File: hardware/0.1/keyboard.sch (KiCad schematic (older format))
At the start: 329 parts, among them J1 USB_C_Receptacle_USB2.0, J2 SWD, Q1 BSS138, Q3 DTC123J, SW1 SW_Push, U1 USBLC6-2SC6, U2 AP2112K-3.3, U3 STM32F303RCTx, Y1 8MHz

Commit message: add encoder top right
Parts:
- removed K_19: KEYSW, josh-keyboard:MXOnly-1U-NoLED, symbol josh-keyboard:MX-NoLED
- removed R7: 1K5, Resistor_SMD:R_0603_1608Metric, symbol Device:R
- added C31, C41: 100n, Capacitor_SMD:C_0603_1608Metric, symbol Device:C
- added K_19: Encoder_MX, josh-keyboard:MX_KEYSWITCH_ENCODER, symbol Device:Rotary_Encoder_Switch
- added RN5: 10K, Resistor_SMD:R_Array_Convex_4x0603, symbol josh-passive:RN
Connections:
- net +3V3: now also RN5.2, RN5.3
- net GND: now also C31.2, C41.2, K_19.C
- net col13: now also U3.17 (PA3); no longer U3.21 (PA5)
- net col19: now also K_19.S1
- net at D_19.2 (A): now also K_19.S2
- net ENC4_A_DB: now reaches U3.58 (PB6)
- net ENC4_A_DB: now also C31.1, RN5.4
- net ENC4_B_DB: now reaches U3.59 (PB7)
- net ENC4_B_DB: now also C41.1, RN5.1
- net MCU_RST: no longer names the net of U3.50 (PA15)
- new net ENC4_A: K_19.A, RN5.5, RN5.6
- new net ENC4_B: K_19.B, RN5.7, RN5.8
- no-connect marks 12 -> 11
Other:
- moved on the sheet: C10, C11, C12, C13, C6, C7, C8, C9, D_107, D_19, D_38, D_58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

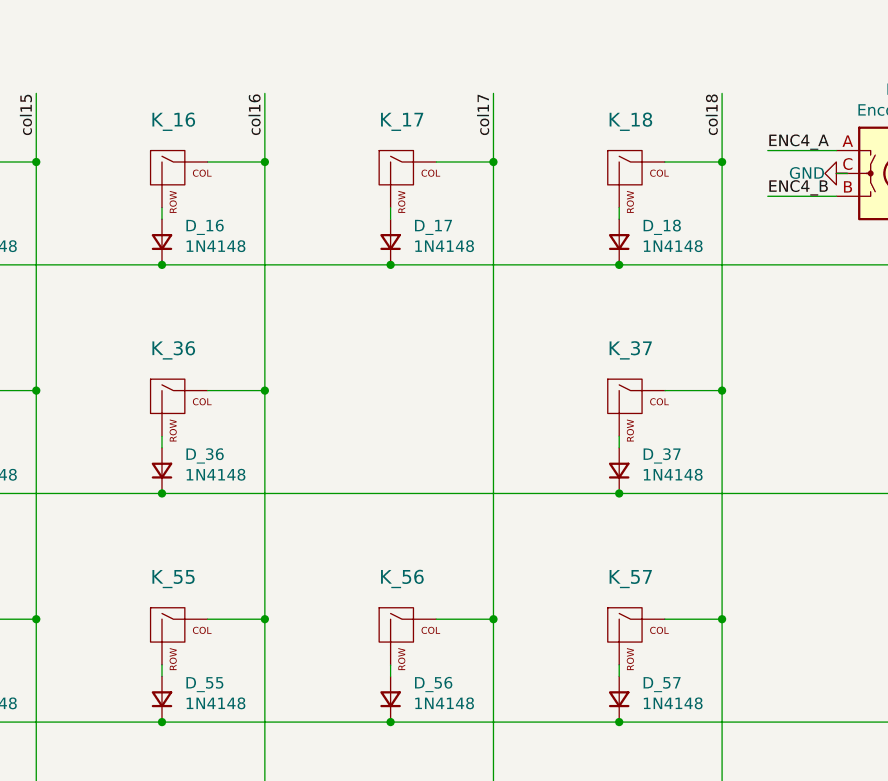
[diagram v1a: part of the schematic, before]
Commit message: add split backspace
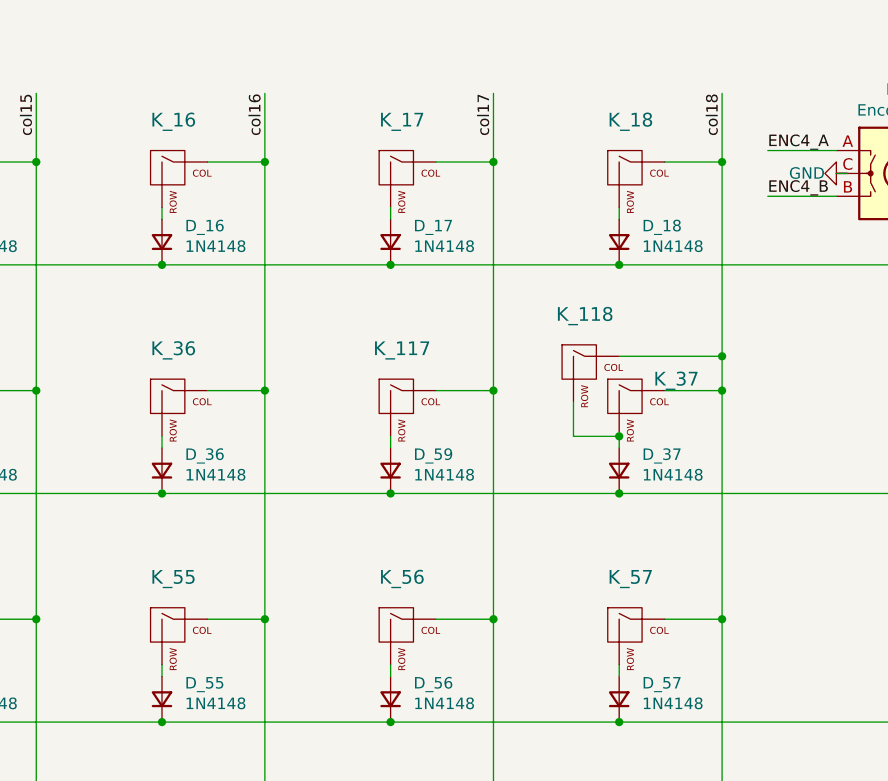
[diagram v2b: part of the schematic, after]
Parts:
- added D_59: 1N4148, Diode_SMD:D_SOD-123, symbol Device:D_Small
- added K_117, K_118: KEYSW, josh-keyboard:MXOnly-1U-NoLED, symbol josh-keyboard:MX-NoLED
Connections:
- net col17: now also K_117.1 (COL)
- net col18: now also K_118.1 (COL)
- net row1: now also D_59.1 (K)
- net at D_37.2 (A), K_37.2 (ROW): now also K_118.2 (ROW)
- new net: D_59.2 (A), K_117.2 (ROW)
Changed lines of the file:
@@
 Connection ~ 6200 3850
 $Comp
-L josh-keyboard:MX-NoLED K_44
-U 1 1 00000441
-P 6800 3900
-F 0 "K_44" H 6800 4133 60  0000 C CNN
-F 1 "KEYSW" H 6800 3800 60  0001 C CNN
-F 2 "josh-keyboard:MXOnly-1.5U-NoLED" H 6800 3900 60  0001 C CNN
-F 3 "" H 6800 3900 60  0000 C CNN
-F 4 "DNP" H 6800 3900 50  0001 C CNN "DNP"
-	1    6800 3900
-	1    0    0    -1
-$EndComp
-$Comp
 L Device:D_Small D_44
 U 1 1 00000440
@@
 	5750 4300 6750 4300
 Wire Wire Line
-	7200 3850 7200 2850
-Wire Wire Line
 	8750 4300 9750 4300
 Wire Wire Line
@@
 Connection ~ 21200 1850
 Wire Wire Line
-	18750 3300 20750 3300
+	18750 3300 19750 3300
 Wire Wire Line
-	21200 1850 21200 2850
+	21200 1850 21200 2700
 Wire Wire Line
 	22050 3050 22050 3100
@@
 U 1 1 00000371
 P 20800 2900
-F 0 "K_37" H 20800 3133 60  0000 C CNN
+F 0 "K_37" H 21000 3000 60  0000 C CNN
 F 1 "KEYSW" H 20800 2800 60  0001 C CNN
 F 2 "josh-keyboard:MXOnly-2U-NoLED" H 20800 2900 60  0001 C CNN
@@
 	6750 4300 8750 4300
 Wire Wire Line
-	20200 1850 20200 3850
+	20200 1850 20200 2850
 Wire Wire Line
 	21200 5850 21200 3850
@@
 	-1   0    0    -1
 $EndComp
+Wire Wire Line
+	19750 3050 19750 3100
+Wire Wire Line
+	19950 2850 20200 2850
+$Comp
+L Device:D_Small D_59
+U 1 1 5F939D73
+P 19750 3200
+F 0 "D_59" V 19820 3100 50  0000 R CNN
+F 1 "1N4148" V 19730 3100 50  0000 R CNN
+F 2 "Diode_SMD:D_SOD-123" H 19450 3150 50  0001 C CNN
+F 3 "~" H 19450 3150 50  0001 C CNN
+F 4 "C81598" H 19750 3200 50  0001 C CNN "JLCSMT"
+F 5 "C81598" H 19750 3200 50  0001 C CNN "LCSC"
+F 6 "1N4148W" H 19750 3200 50  0001 C CNN "MPN"
+F 7 "Semtech" H 19750 3200 50  0001 C CNN "Manufacturer"
+	1    19750 3200
+	0    -1   -1   0
+$EndComp
+Connection ~ 19750 3300
+Wire Wire Line
+	19750 3300 20750 3300
+Connection ~ 20200 2850
+Wire Wire Line
+	20200 2850 20200 3850
+Wire Wire Line
+	20550 2900 20550 3050
+Wire Wire Line
+	20550 3050 20750 3050
+Connection ~ 20750 3050
+Wire Wire Line
+	20750 2700 21200 2700
+Connection ~ 21200 2700
+Wire Wire Line
+	21200 2700 21200 2850
+$Comp
+L josh-keyboard:MX-NoLED K_117
+U 1 1 5FB78AAD
+P 19800 2900
+F 0 "K_117" H 19800 3133 60  0000 C CNN
+F 1 "KEYSW" H 19800 2800 60  0001 C CNN
+F 2 "josh-keyboard:MXOnly-1U-NoLED" H 19800 2900 60  0001 C CNN
+F 3 "" H 19800 2900 60  0000 C CNN
+F 4 "DNP" H 19800 2900 50  0001 C CNN "DNP"
+	1    19800 2900
+	1    0    0    -1
+$EndComp
+$Comp
+L josh-keyboard:MX-NoLED K_118
+U 1 1 5FB78FEA
+P 20600 2750
+F 0 "K_118" H 20600 2983 60  0000 C CNN
+F 1 "KEYSW" H 20600 2650 60  0001 C CNN
+F 2 "josh-keyboard:MXOnly-1U-NoLED" H 20600 2750 60  0001 C CNN
+F 3 "" H 20600 2750 60  0000 C CNN
+F 4 "DNP" H 20600 2750 50  0001 C CNN "DNP"
+	1    20600 2750
+	1    0    0    -1
+$EndComp
+Wire Wire Line
+	7200 3850 7200 2850
+$Comp
+L josh-keyboard:MX-NoLED K_44
+U 1 1 00000441
+P 6800 3900
+F 0 "K_44" H 6800 4133 60  0000 C CNN
+F 1 "KEYSW" H 6800 3800 60  0001 C CNN
+F 2 "josh-keyboard:MXOnly-1.5U-NoLED" H 6800 3900 60  0001 C CNN
+F 3 "" H 6800 3900 60  0000 C CNN
+F 4 "DNP" H 6800 3900 50  0001 C CNN "DNP"
+	1    6800 3900
+	1    0    0    -1
+$EndComp
 $EndSCHEMATC

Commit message: off to fab
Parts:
- C3, C40: JLCSMT C19702 -> 1740133; LCSC C19702 -> 1740133; MPN CL10A106KP8NNNC -> (none)
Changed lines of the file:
@@
 F 2 "Capacitor_SMD:C_0603_1608Metric" H 12188 15350 50  0001 C CNN
 F 3 "~" H 12150 15500 50  0001 C CNN
-F 4 "C19702" H 12150 15500 50  0001 C CNN "JLCSMT"
-F 5 "C19702" H 12150 15500 50  0001 C CNN "LCSC"
-F 6 "CL10A106KP8NNNC" H 12150 15500 50  0001 C CNN "MPN"
+F 4 "1740133" H 12150 15500 50  0001 C CNN "JLCSMT"
+F 5 "1740133" H 12150 15500 50  0001 C CNN "LCSC"
+F 6 "" H 12150 15500 50  0001 C CNN "MPN"
 F 7 "Samsung Electro-Mechanics" H 12150 15500 50  0001 C CNN "Manufacturer"
 	1    12150 15500
@@
 F 2 "Capacitor_SMD:C_0603_1608Metric" H 2788 8800 50  0001 C CNN
 F 3 "~" H 2750 8950 50  0001 C CNN
-F 4 "C19702" H 2750 8950 50  0001 C CNN "JLCSMT"
-F 5 "C19702" H 2750 8950 50  0001 C CNN "LCSC"
-F 6 "CL10A106KP8NNNC" H 2750 8950 50  0001 C CNN "MPN"
+F 4 "1740133" H 2750 8950 50  0001 C CNN "JLCSMT"
+F 5 "1740133" H 2750 8950 50  0001 C CNN "LCSC"
+F 6 "" H 2750 8950 50  0001 C CNN "MPN"
 F 7 "Samsung Electro-Mechanics" H 2750 8950 50  0001 C CNN "Manufacturer"
 	1    2750 8950
